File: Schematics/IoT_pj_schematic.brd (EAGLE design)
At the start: 58.8 x 37.1 mm, 109 parts, among them J1 -, J6 -, J7 -, Q1 2N7002, Q2 SIA817, Q3 2N7002, Q5 2N7002DW-7-FNO_PAD, U1 D21G18, U2 SN74AVC4T774, U3 SARA-U201, U5 BQ24195L, U6 AP721533, U7 SN74AVC4T774, Y1 32768Hz

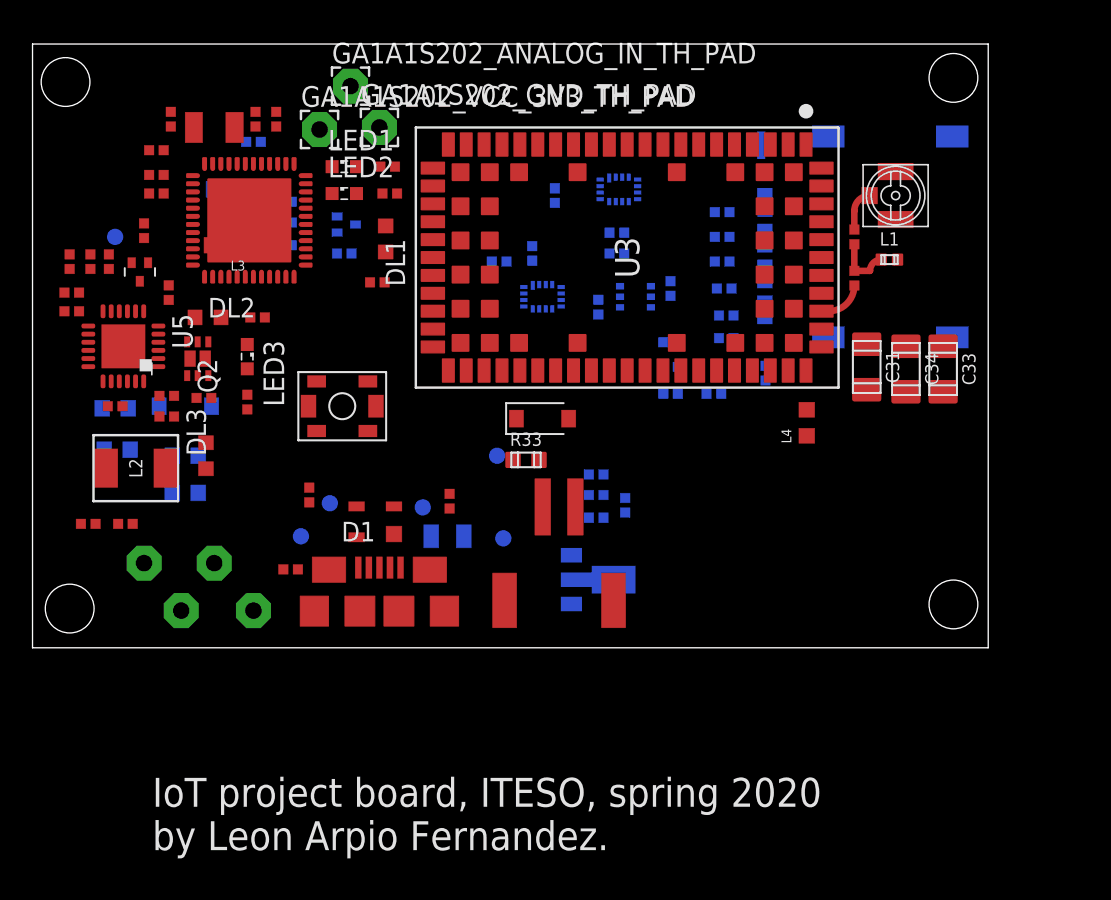
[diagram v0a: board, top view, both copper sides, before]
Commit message: Add: Board fully routed
2-layer board
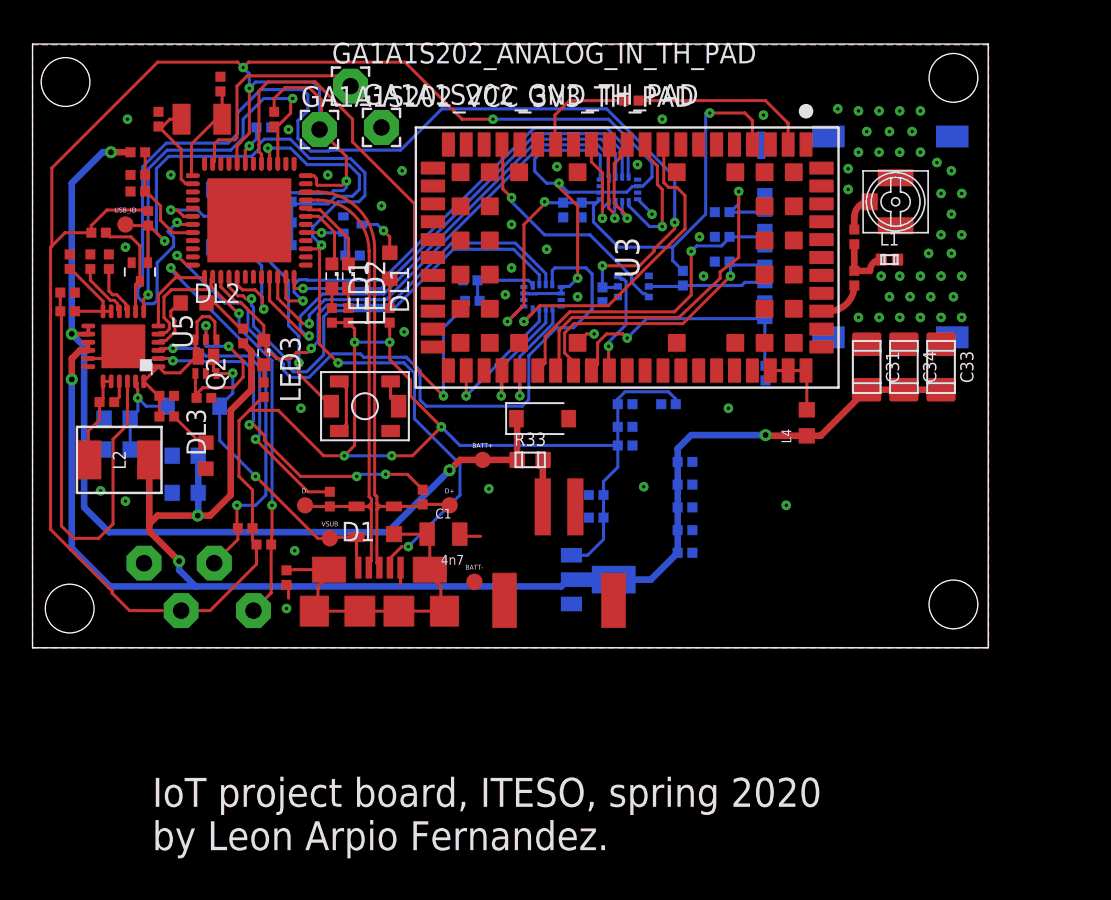
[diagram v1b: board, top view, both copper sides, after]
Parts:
- moved C8 13.1 mm to (36.4, 12.4), turned to 0 degrees
- moved C30 13.0 mm to (40.1, 5.84)
- moved C37 12.3 mm to (40.1, 10.0), turned to 180 degrees
- moved C36 11.9 mm to (32.6, 26.9), turned to 270 degrees
- moved R6 9.77 mm to (18.4, 20.4), turned to 90 degrees
- moved R14 9.66 mm to (13.1, 7.37)
- moved R13 8.60 mm to (14.2, 6.35), turned to 180 degrees
- moved C35 8.28 mm to (36.4, 13.6), turned to 0 degrees
- moved R2 7.91 mm to (19.4, 20.4), turned to 90 degrees
- moved R12 7.50 mm to (36.8, 33.7), flipped to the top, turned to 0 degrees
- moved C28 7.04 mm to (40.1, 8.64)
- moved LED1 6.77 mm to (18.4, 22.9), turned to 270 degrees
- moved C24 6.20 mm to (39.1, 15.0)
- moved C29 5.91 mm to (40.1, 11.4)
- moved R26 5.68 mm to (4.06, 25.5), turned to 0 degrees
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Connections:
- net PA07_AIN7: now also U1.12
- net PA11_TCC0-W3: now also U1.16
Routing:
- net +3V3: track 0.00 -> 229.3 mm, vias 0 -> 12
- net +3V8: track 0.00 -> 105.1 mm, vias 0 -> 4
- net PB08_RST: track 0.00 -> 69.3 mm, vias 0 -> 3
- net PA18_OTG: track 0.00 -> 60.0 mm, vias 0 -> 4
- net VBATT: track 0.00 -> 57.8 mm, vias 0 -> 3
- net PA07_AIN7: track 0.00 -> 43.5 mm, vias 0 -> 1
- net PA28_S2_DTR: track 0.00 -> 37.2 mm, vias 0 -> 1
- net +1V8: track 0.00 -> 35.7 mm, vias 0 -> 3
- net PA12_S2_TX: track 0.00 -> 32.1 mm, vias 0 -> 1
- net PA14_S2_RTS: track 0.00 -> 30.5 mm, vias 0 -> 1
- net USB_P: track 0.00 -> 30.3 mm
- net USB_N: track 0.00 -> 29.2 mm
- net PA10_TCC0-W2: track 0.00 -> 29.0 mm, vias 0 -> 1
- net PA13_S2_RX: track 0.00 -> 28.8 mm, vias 0 -> 1
- net PA11_TCC0-W3: track 0.00 -> 28.7 mm, vias 0 -> 1
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- added copper zone on layer 1, net GND
- added copper zone on layer 16, net GND

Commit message: FIx: Silkscreen names and values corrected
Corrected the position so they wouldn't overlap
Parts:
- renumbered GA1A1S202_ANALOG_IN_TH_PAD to A_IN, GA1A1S202_GND_TH_PAD to GND, GA1A1S202_VCC_3V3_TH_PAD to VCC, I2C_GND_TH_PAD to GND_, I2C_SCL_TH_PAD to SCL, I2C_SDA_TH_PAD to SDA, I2C_VCC_3V3_TH_PAD to VCC_, LED1 to GSM_CN, LED2 to PUBLISH
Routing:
- net GND: vias 67 -> 68
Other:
- board text added: "J6"
